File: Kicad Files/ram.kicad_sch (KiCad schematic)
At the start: 30 parts

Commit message: started tidy up in control
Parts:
- gave numbers to parts that had none: 25

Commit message: work on cl
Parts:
- C11: renamed from C15; value 10nF -> C_Small
- C12: renamed from C13; value 0.1µF -> C
- C13: renamed from C14; value 0.1µF -> C
- R54: renamed from R125; value 1k -> R_Small
- R55: renamed from R117; value 220 -> R
- R56: renamed from R118; value 220 -> R
- R57: renamed from R119; value 220 -> R
- R58: renamed from R120; value 220 -> R
- R59: renamed from R121; value 220 -> R
- R60: renamed from R122; value 220 -> R
- R61: renamed from R123; value 220 -> R
- R62: renamed from R124; value 220 -> R
- gave numbers to parts that had none: 2
- renumbered D88 to D24, D89 to D25, D90 to D26, D91 to D27, D92 to D28, D93 to D29, D94 to D30, D95 to D31, U55 to U19, U51 to U20, U53 to U21, U52 to U22

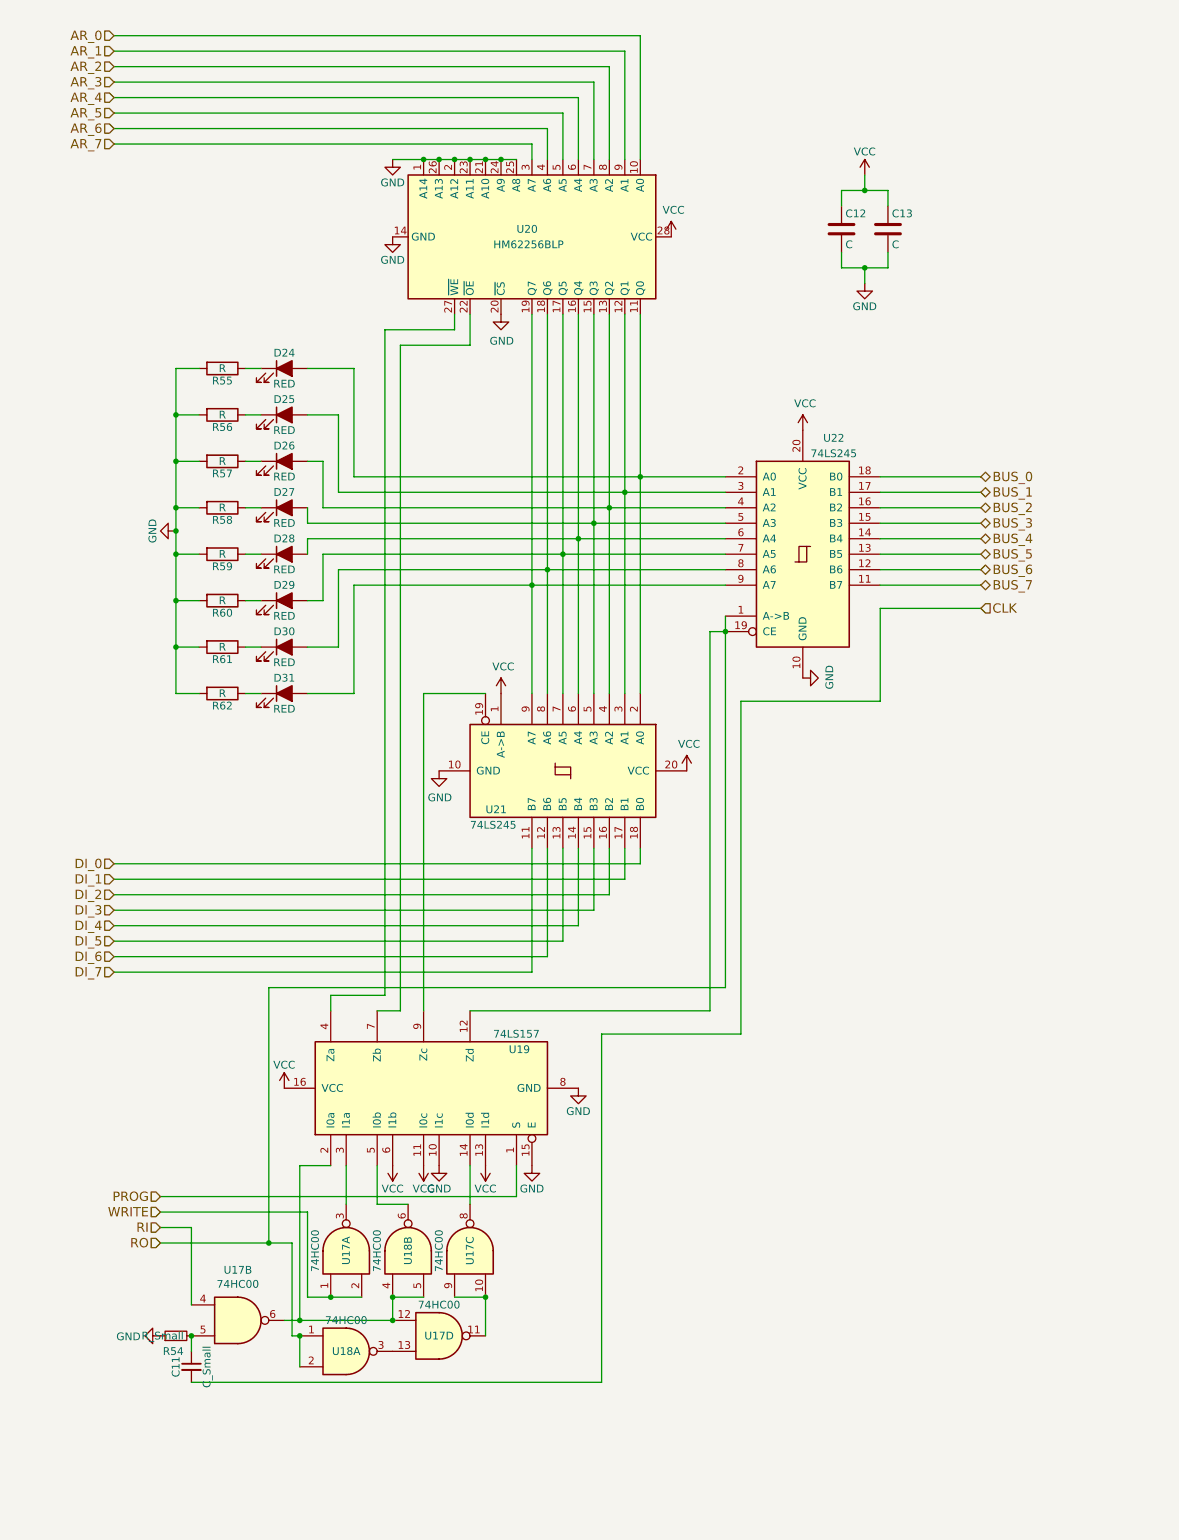
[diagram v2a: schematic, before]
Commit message: changed to 16bit Addr Bus
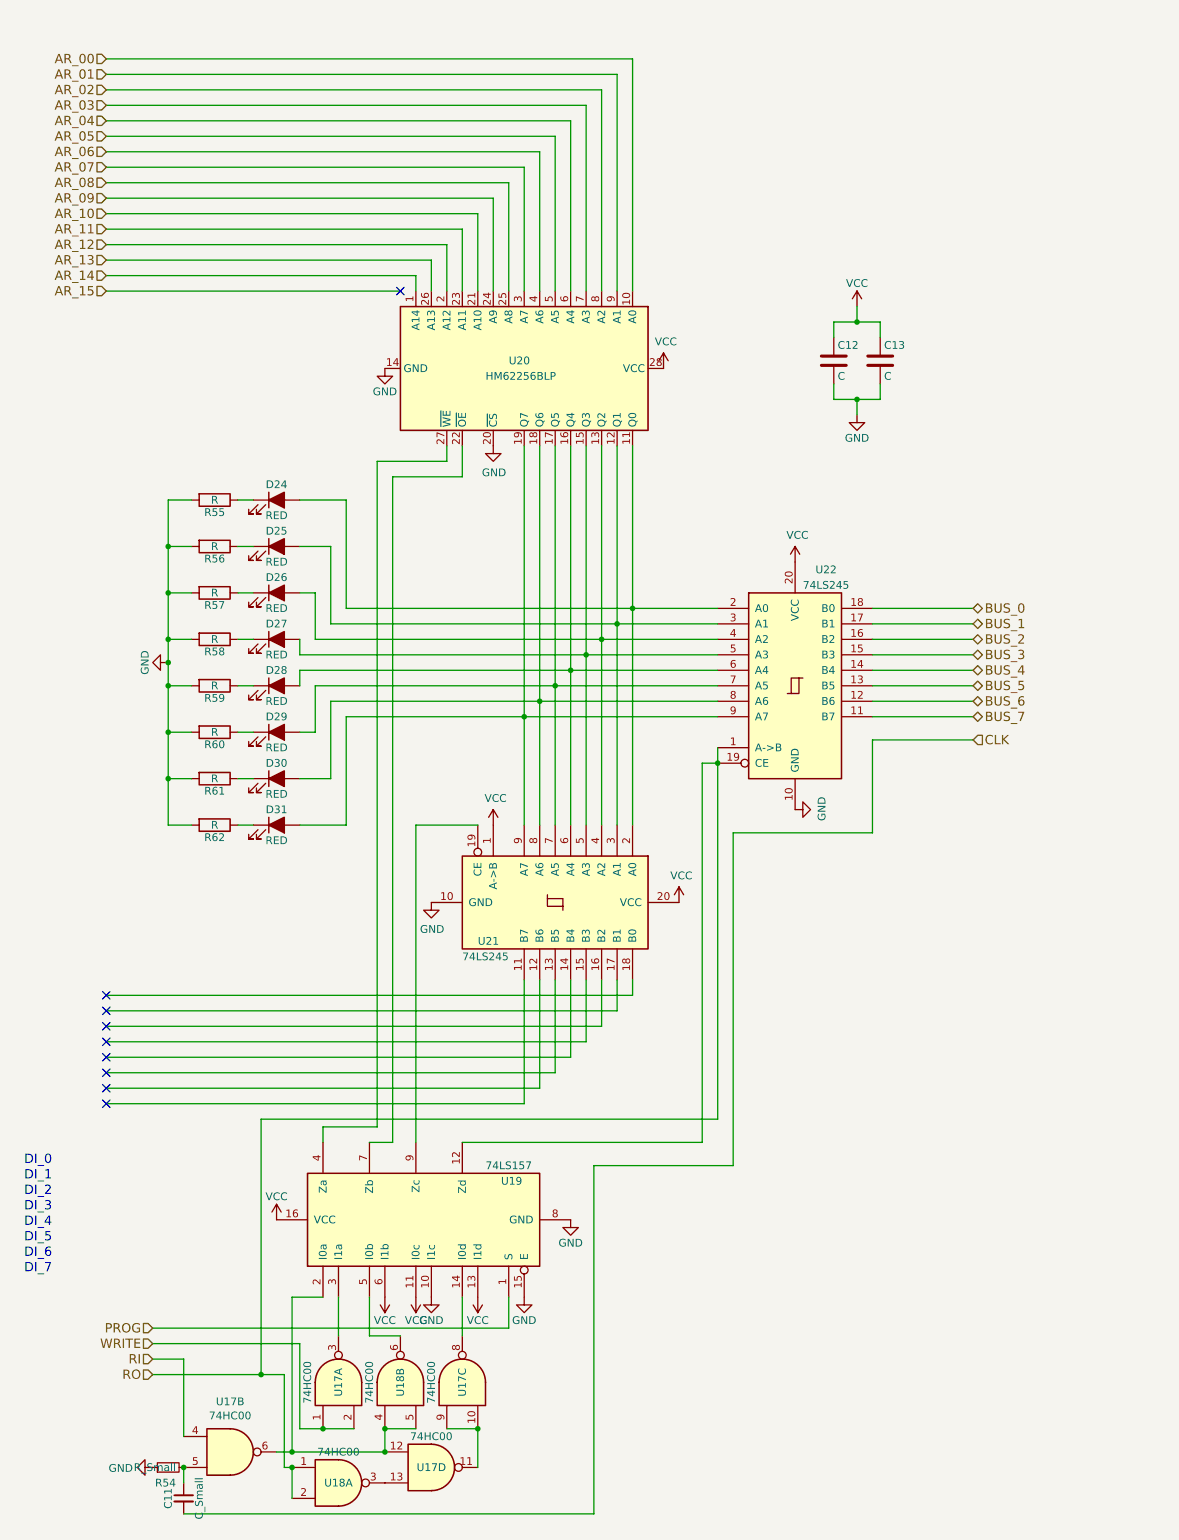
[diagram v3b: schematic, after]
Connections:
- net GND: no longer U20.1 (A14), U20.2 (A12), U20.21 (A10), U20.23 (A11), U20.24 (A9), U20.25 (A8), U20.26 (A13)
- net AR_0 renamed AR_00
- net AR_1 renamed AR_01
- net AR_2 renamed AR_02
- net AR_3 renamed AR_03
- net AR_4 renamed AR_04
- net AR_5 renamed AR_05
- net AR_6 renamed AR_06
- net AR_7 renamed AR_07
- net DI_0: no longer names the net of U21.18 (B0)
- net DI_1: no longer names the net of U21.17 (B1)
- net DI_2: no longer names the net of U21.16 (B2)
- net DI_3: no longer names the net of U21.15 (B3)
- net DI_4: no longer names the net of U21.14 (B4)
- net DI_5: no longer names the net of U21.13 (B5)
- net DI_6: no longer names the net of U21.12 (B6)
- net DI_7: no longer names the net of U21.11 (B7)
- new net AR_08: U20.25 (A8)
- new net AR_09: U20.24 (A9)
- new net AR_10: U20.21 (A10)
- new net AR_11: U20.23 (A11)
- new net AR_12: U20.2 (A12)
- new net AR_13: U20.26 (A13)
- new net AR_14: U20.1 (A14)
- no-connect marks 0 -> 9
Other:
- note added: "DI_0"
- note added: "DI_1"
- note added: "DI_2"
- note added: "DI_3"
- note added: "DI_4"
- note added: "DI_5"
- note added: "DI_6"
- note added: "DI_7"
- moved on the sheet: C11, C12, C13, D24, D25, D26, D27, D28, D29, D30, D31, R54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

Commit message: w1
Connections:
- net AR_00 renamed ABUS_00
- net AR_01 renamed ABUS_01
- net AR_02 renamed ABUS_02
- net AR_03 renamed ABUS_03
- net AR_04 renamed ABUS_04
- net AR_05 renamed ABUS_05
- net AR_06 renamed ABUS_06
- net AR_07 renamed ABUS_07
- net AR_08 renamed ABUS_08
- net AR_09 renamed ABUS_09
- net AR_10 renamed ABUS_10
- net AR_11 renamed ABUS_11
- net AR_12 renamed ABUS_12
- net AR_13 renamed ABUS_13
- net AR_14 renamed ABUS_14
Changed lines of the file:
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@@
     (effects (font (size 1.524 1.524)) (justify right bottom))
   )
-  (hierarchical_label "AR_09" (shape input) (at 33.02 45.72 180)
+  (hierarchical_label "ABUS_15" (shape input) (at 33.02 60.96 180)
+    (effects (font (size 1.524 1.524)) (justify right))
+  )
+  (hierarchical_label "ABUS_14" (shape input) (at 33.02 58.42 180)
     (effects (font (size 1.524 1.524)) (justify right))
   )
@@
     (effects (font (size 1.524 1.524)) (justify right))
   )
+  (hierarchical_label "ABUS_09" (shape input) (at 33.02 45.72 180)
+    (effects (font (size 1.524 1.524)) (justify right))
+  )
   (hierarchical_label "CLK" (shape input) (at 175.26 134.62 0)
     (effects (font (size 1.524 1.524)) (justify left))
@@
     (effects (font (size 1.524 1.524)) (justify left))
   )
-  (hierarchical_label "AR_03" (shape input) (at 33.02 30.48 180)
+  (hierarchical_label "ABUS_10" (shape input) (at 33.02 48.26 180)
     (effects (font (size 1.524 1.524)) (justify right))
   )
-  (hierarchical_label "AR_06" (shape input) (at 33.02 38.1 180)
+  (hierarchical_label "ABUS_08" (shape input) (at 33.02 43.18 180)
     (effects (font (size 1.524 1.524)) (justify right))
   )
-  (hierarchical_label "AR_00" (shape input) (at 33.02 22.86 180)
-    (effects (font (size 1.524 1.524)) (justify right))
-  )
-  (hierarchical_label "AR_14" (shape input) (at 33.02 58.42 180)
-    (effects (font (size 1.524 1.524)) (justify right))
-  )
-  (hierarchical_label "AR_04" (shape input) (at 33.02 33.02 180)
+  (hierarchical_label "ABUS_01" (shape input) (at 33.02 25.4 180)
     (effects (font (size 1.524 1.524)) (justify right))
   )
@@
     (effects (font (size 1.524 1.524)) (justify right))
   )
+  (hierarchical_label "ABUS_05" (shape input) (at 33.02 35.56 180)
+    (effects (font (size 1.524 1.524)) (justify right))
+  )
   (hierarchical_label "BUS_2" (shape tri_state) (at 175.26 118.11 0)
     (effects (font (size 1.524 1.524)) (justify left))
   )
-  (hierarchical_label "AR_05" (shape input) (at 33.02 35.56 180)
+  (hierarchical_label "ABUS_04" (shape input) (at 33.02 33.02 180)
     (effects (font (size 1.524 1.524)) (justify right))
   )
-  (hierarchical_label "AR_01" (shape input) (at 33.02 25.4 180)
+  (hierarchical_label "ABUS_13" (shape input) (at 33.02 55.88 180)
     (effects (font (size 1.524 1.524)) (justify right))
   )
-  (hierarchical_label "AR_11" (shape input) (at 33.02 50.8 180)
+  (hierarchical_label "ABUS_11" (shape input) (at 33.02 50.8 180)
     (effects (font (size 1.524 1.524)) (justify right))
   )
-  (hierarchical_label "AR_08" (shape input) (at 33.02 43.18 180)
+  (hierarchical_label "ABUS_03" (shape input) (at 33.02 30.48 180)
+    (effects (font (size 1.524 1.524)) (justify right))
+  )
+  (hierarchical_label "ABUS_02" (shape input) (at 33.02 27.94 180)
+    (effects (font (size 1.524 1.524)) (justify right))
+  )
+  (hierarchical_label "ABUS_00" (shape input) (at 33.02 22.86 180)
+    (effects (font (size 1.524 1.524)) (justify right))
+  )
+  (hierarchical_label "ABUS_12" (shape input) (at 33.02 53.34 180)
     (effects (font (size 1.524 1.524)) (justify right))
   )
@@
     (effects (font (size 1.524 1.524)) (justify left))
   )
-  (hierarchical_label "AR_15" (shape input) (at 33.02 60.96 180)
+  (hierarchical_label "ABUS_06" (shape input) (at 33.02 38.1 180)
     (effects (font (size 1.524 1.524)) (justify right))
   )
-  (hierarchical_label "AR_07" (shape input) (at 33.02 40.64 180)
-    (effects (font (size 1.524 1.524)) (justify right))
-  )
-  (hierarchical_label "AR_02" (shape input) (at 33.02 27.94 180)
+  (hierarchical_label "ABUS_07" (shape input) (at 33.02 40.64 180)
     (effects (font (size 1.524 1.524)) (justify right))
   )
   (hierarchical_label "RO" (shape input) (at 40.64 238.76 180)
-    (effects (font (size 1.524 1.524)) (justify right))
-  )
-  (hierarchical_label "AR_10" (shape input) (at 33.02 48.26 180)
-    (effects (font (size 1.524 1.524)) (justify right))
-  )
-  (hierarchical_label "AR_13" (shape input) (at 33.02 55.88 180)
     (effects (font (size 1.524 1.524)) (justify right))
   )
@@
     (effects (font (size 1.524 1.524)) (justify left))
   )
-  (hierarchical_label "AR_12" (shape input) (at 33.02 53.34 180)
-    (effects (font (size 1.524 1.524)) (justify right))
-  )
   (symbol (lib_id "8bit-computer-rescue:LED_ALT-Device") (at 60.96 148.59 0) (unit 1)

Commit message: work on pc2
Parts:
- removed C11: C_Small, symbol Device:C_Small
- removed D24, D25, D26, D27, D28, D29, D30, D31: RED, LED_THT:LED_D5.0mm, symbol 8bit-computer-rescue:LED_ALT-Device
- removed R54: R_Small, symbol Device:R_Small
- removed R55, R56, R57, R58, R59, R60, R61, R62: R, Resistor_THT:R_Axial_DIN0207_L6.3mm_D2.5mm_P7.62mm_Horizontal, symbol Device:R
- removed U17, U18: 74HC00, symbol 74xx:74HC00
- removed U19: 74LS157, symbol 74xx:74LS157
- removed U21: 74LS245, symbol 74xx:74LS245
- added D? (x8): LED, symbol Device:LED
- added R? (x8): R_Small, symbol Device:R_Small
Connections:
- net GND: now also U20.22 (~{OE}), R?.2, R?.2, R?.2, R?.2, R?.2, R?.2, R?.2, R?.2
- net at U20.19 (Q7), U22.9 (A7): now also D?.2 (A)
- net at U20.18 (Q6), U22.8 (A6): now also D?.2 (A)
- net at U20.17 (Q5), U22.7 (A5): now also D?.2 (A)
- net at U20.16 (Q4), U22.6 (A4): now also D?.2 (A)
- net at U20.15 (Q3), U22.5 (A3): now also D?.2 (A)
- net at U20.13 (Q2), U22.4 (A2): now also D?.2 (A)
- net at U20.12 (Q1), U22.3 (A1): now also D?.2 (A)
- net at U20.11 (Q0), U22.2 (A0): now also D?.2 (A)
- net ~{RI}: now reaches U20.27 (~{WE})
- net ~{RI}: now also U22.1 (A->B)
- net RO renamed ~{RO}
- net ~{RO}: no longer U22.1 (A->B)
- new net: D?.1 (K), R?.1 (x8)
- no-connect marks 9 -> 1
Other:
- note removed: "DI_0"
- note removed: "DI_1"
- note removed: "DI_2"
- note removed: "DI_3"
- note removed: "DI_4"
- note removed: "DI_5"
- note removed: "DI_6"
- note removed: "DI_7"
- moved on the sheet: C12, C13, U20, U22
